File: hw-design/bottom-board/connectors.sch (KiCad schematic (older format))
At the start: 24 parts, among them J1 JACK_TRS_6PINS, J2 JACK_TRS_6PINS, J3 JACK_TRS_6PINS, J4 JACK_TRS_6PINS, J5 JACK_TRS_6PINS, J6 RJ45_LEDS, P5 BARREL_JACK, P6 HMI_POWER, P7 SD_CARD, P8 HMI_DATA, P9 SERIAL_DEBUG

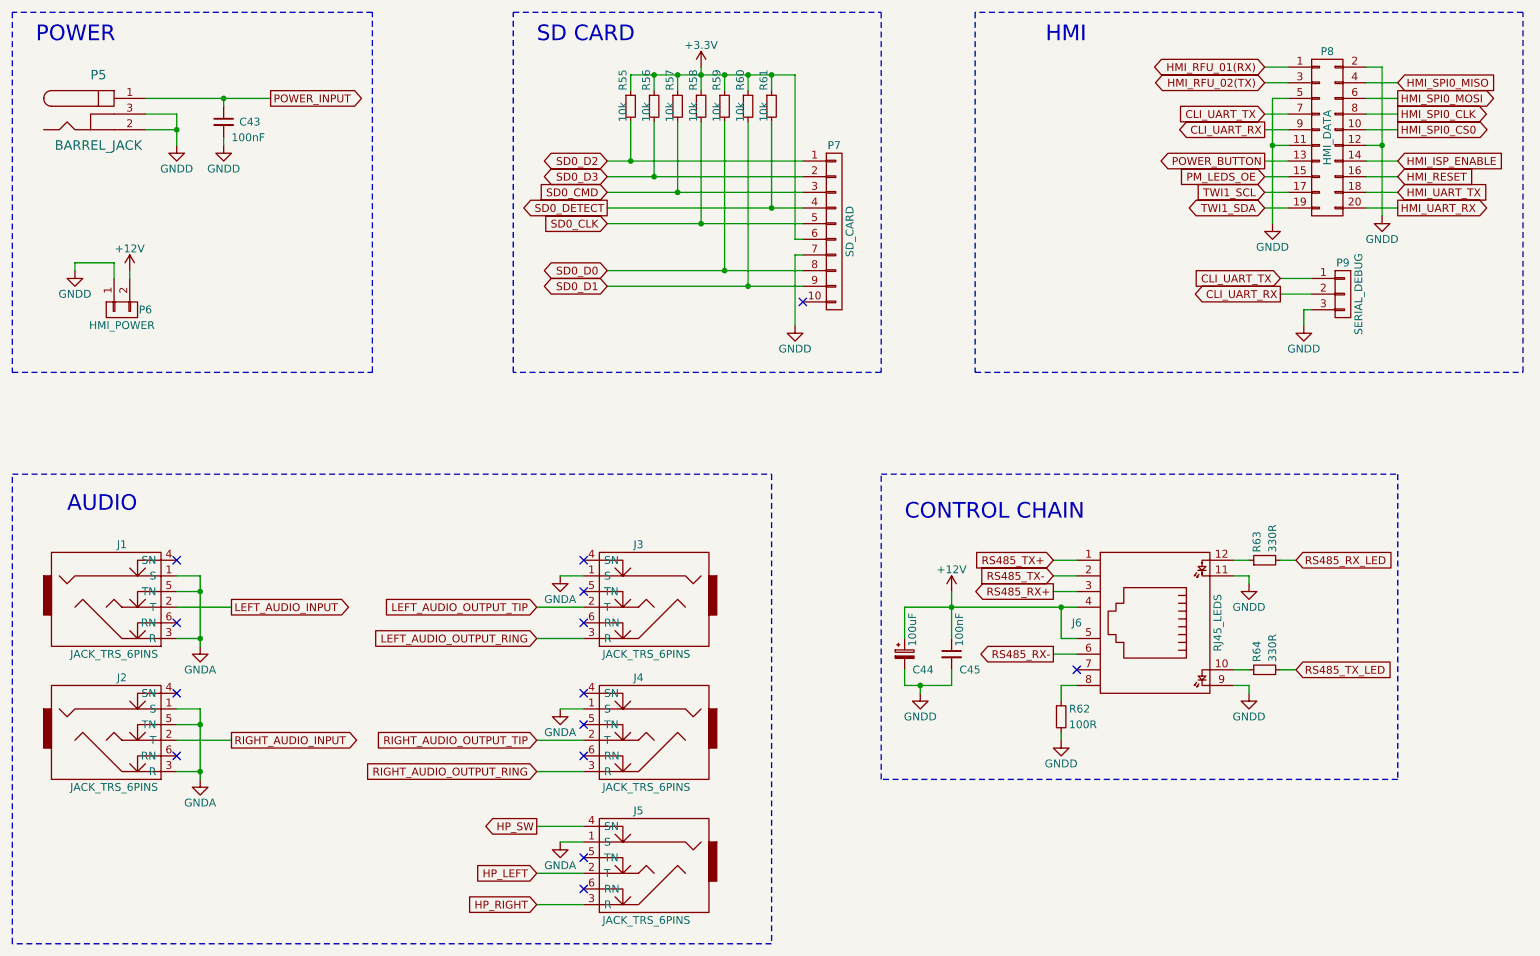
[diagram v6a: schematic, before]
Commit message: bottom-board,pcb: adding protection resistors to UART CLI
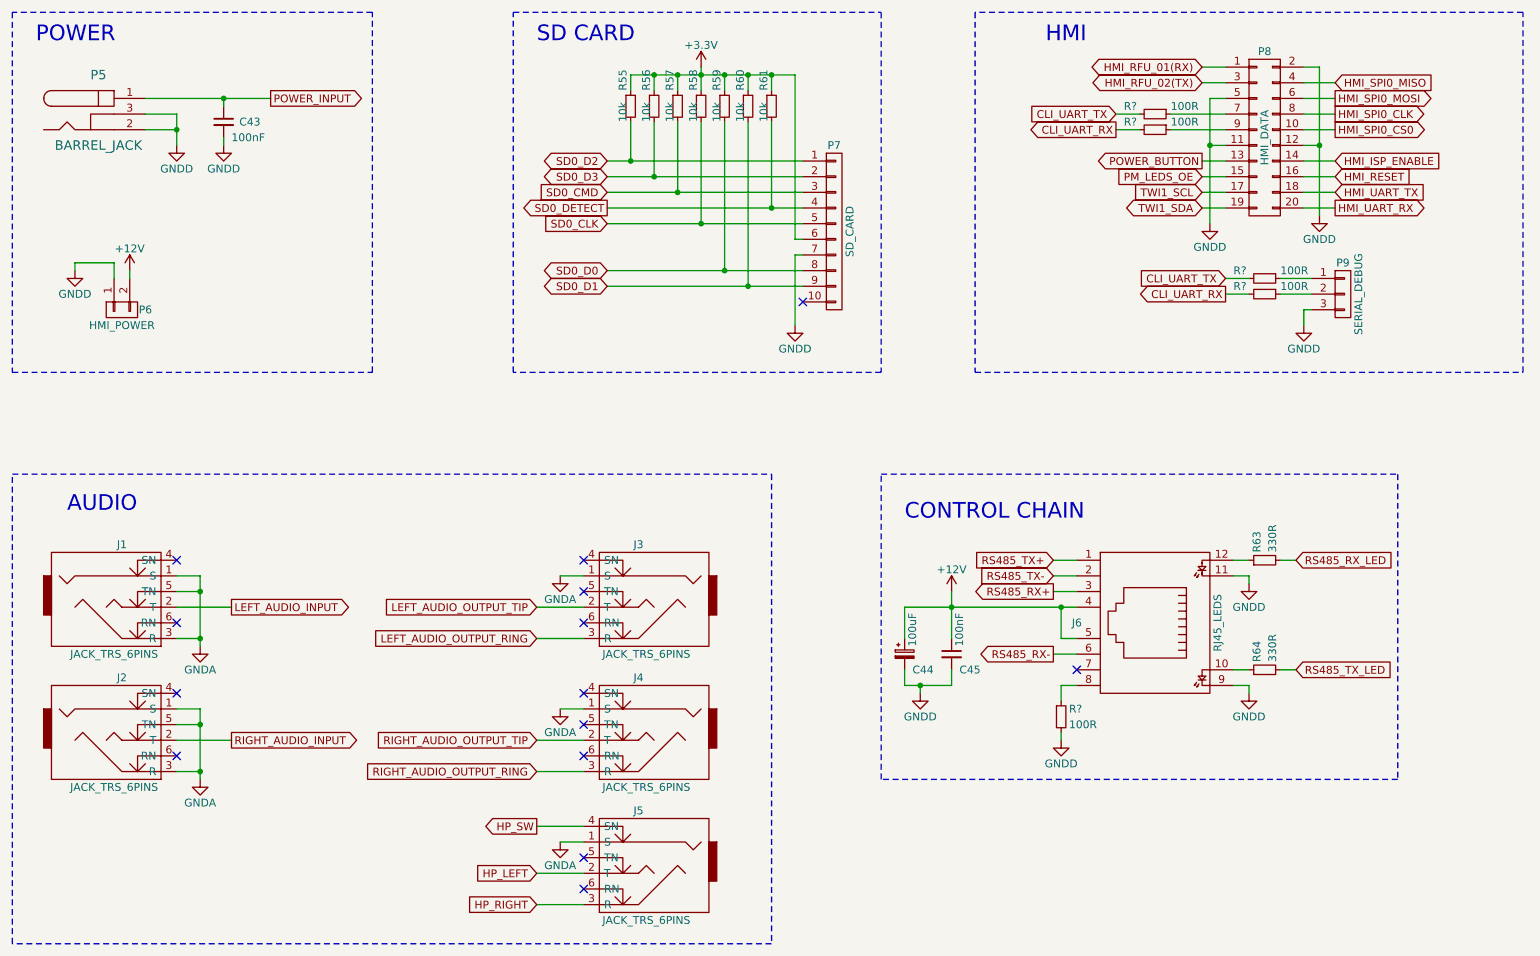
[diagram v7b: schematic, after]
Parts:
- removed R62: 100R, Resistors_SMD:R_0603, symbol R_Small
- added R? (x4): 100R, Resistors_SMD:R_0603, symbol R_Small
- added R?: 100R, Resistors_SMD:R_0805, symbol R_Small
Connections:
- net CLI_UART_RX: now also R?.2, R?.2; no longer P8.9 (P9), P9.2 (P2)
- net CLI_UART_TX: now also R?.2, R?.2; no longer P8.7 (P7), P9.1 (P1)
- net GNDD: now also R?.2
- net at J6.8: now also R?.1
- new net: P8.7 (P7), R?.1
- new net: P8.9 (P9), R?.1
- new net: P9.1 (P1), R?.1
- new net: P9.2 (P2), R?.1
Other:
- moved on the sheet: P8
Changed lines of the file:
@@
 L CONN_02X10 P8
 U 1 1 550C4B50
-P 9650 1650
-F 0 "P8" H 9650 2200 50  0000 C CNN
-F 1 "HMI_DATA" V 9650 1650 50  0000 C CNN
-F 2 "footprints:Pin_Header_Straight_2x10_Shrouded" H 9650 450 60  0001 C CNN
-F 3 "" H 9650 450 60  0000 C CNN
-F 4 "SBH11-PBPC-D10-ST-BK" H 450 -150 50  0001 C CNN "MPN"
-	1    9650 1650
+P 9250 1650
+F 0 "P8" H 9250 2200 50  0000 C CNN
+F 1 "HMI_DATA" V 9250 1650 50  0000 C CNN
+F 2 "footprints:Pin_Header_Straight_2x10_Shrouded" H 9250 450 60  0001 C CNN
+F 3 "" H 9250 450 60  0000 C CNN
+F 4 "SBH11-PBPC-D10-ST-BK" H 50  -150 50  0001 C CNN "MPN"
+	1    9250 1650
 	1    0    0    -1
 $EndComp
@@
 $EndComp
 $Comp
-L R_Small R62
-U 1 1 550C9A10
-P 7950 5350
-F 0 "R62" H 8000 5400 50  0000 L CNN
-F 1 "100R" H 8000 5300 50  0000 L CNN
-F 2 "Resistors_SMD:R_0603" H 7950 5350 60  0001 C CNN
-F 3 "" H 7950 5350 60  0000 C CNN
-F 4 "RMCF0603JT100R" H -800 0   50  0001 C CNN "MPN"
-	1    7950 5350
-	1    0    0    -1
-$EndComp
-$Comp
 L GNDD #PWR0152
 U 1 1 550C9AAB
@@
 L GNDD #PWR0161
 U 1 1 550AE498
-P 9300 2200
-F 0 "#PWR0161" H 9300 1950 50  0001 C CNN
-F 1 "GNDD" H 9300 2050 50  0000 C CNN
-F 2 "" H 9300 2200 60  0000 C CNN
-F 3 "" H 9300 2200 60  0000 C CNN
-	1    9300 2200
+P 8900 2200
+F 0 "#PWR0161" H 8900 1950 50  0001 C CNN
+F 1 "GNDD" H 8900 2050 50  0000 C CNN
+F 2 "" H 8900 2200 60  0000 C CNN
+F 3 "" H 8900 2200 60  0000 C CNN
+	1    8900 2200
 	1    0    0    -1
 $EndComp
@@
 L GNDD #PWR0162
 U 1 1 550B207C
-P 10000 2150
-F 0 "#PWR0162" H 10000 1900 50  0001 C CNN
-F 1 "GNDD" H 10000 2000 50  0000 C CNN
-F 2 "" H 10000 2150 60  0000 C CNN
-F 3 "" H 10000 2150 60  0000 C CNN
-	1    10000 2150
+P 9600 2150
+F 0 "#PWR0162" H 9600 1900 50  0001 C CNN
+F 1 "GNDD" H 9600 2000 50  0000 C CNN
+F 2 "" H 9600 2150 60  0000 C CNN
+F 3 "" H 9600 2150 60  0000 C CNN
+	1    9600 2150
 	1    0    0    -1
 $EndComp
@@
 Text Notes 7850 1050 0    100  ~ 0
 HMI
-Text GLabel 9350 2550 0    50   Input ~ 0
+Text GLabel 9000 2550 0    50   Input ~ 0
 CLI_UART_TX
-Text GLabel 9350 2650 0    50   Output ~ 0
+Text GLabel 9000 2650 0    50   Output ~ 0
 CLI_UART_RX
-Text GLabel 10100 2100 2    50   Output ~ 0
+Text GLabel 9700 2100 2    50   Output ~ 0
 HMI_UART_RX
-Text GLabel 10100 2000 2    50   Input ~ 0
+Text GLabel 9700 2000 2    50   Input ~ 0
 HMI_UART_TX
-Text GLabel 10100 1800 2    50   Input ~ 0
+Text GLabel 9700 1800 2    50   Input ~ 0
 HMI_ISP_ENABLE
-Text GLabel 10100 1900 2    50   Input ~ 0
+Text GLabel 9700 1900 2    50   Input ~ 0
 HMI_RESET
-Text GLabel 9250 1500 0    50   Input ~ 0
+Text GLabel 8300 1500 0    50   Input ~ 0
 CLI_UART_TX
-Text GLabel 9250 1600 0    50   Output ~ 0
+Text GLabel 8300 1600 0    50   Output ~ 0
 CLI_UART_RX
 Text GLabel 5050 2200 0    50   Input ~ 0
@@
 Text Notes 4600 1050 0    100  ~ 0
 SD CARD
-Text GLabel 10100 1300 2    50   Input ~ 0
+Text GLabel 9700 1300 2    50   Input ~ 0
 HMI_SPI0_MISO
-Text GLabel 10100 1500 2    50   Output ~ 0
+Text GLabel 9700 1500 2    50   Output ~ 0
 HMI_SPI0_CLK
-Text GLabel 10100 1600 2    50   Output ~ 0
+Text GLabel 9700 1600 2    50   Output ~ 0
 HMI_SPI0_CS0
-Text GLabel 10100 1400 2    50   Output ~ 0
+Text GLabel 9700 1400 2    50   Output ~ 0
 HMI_SPI0_MOSI
-Text GLabel 9250 1800 0    50   Output ~ 0
+Text GLabel 8850 1800 0    50   Output ~ 0
 POWER_BUTTON
 Text GLabel 9450 5050 2    50   Input ~ 0
@@
 Text GLabel 9450 4350 2    50   Input ~ 0
 RS485_RX_LED
-Text GLabel 9250 2100 0    50   BiDi ~ 0
+Text GLabel 8850 2100 0    50   BiDi ~ 0
 TWI1_SDA
-Text GLabel 9250 2000 0    50   Input ~ 0
+Text GLabel 8850 2000 0    50   Input ~ 0
 TWI1_SCL
-Text GLabel 9250 1200 0    50   BiDi ~ 0
+Text GLabel 8850 1200 0    50   BiDi ~ 0
 HMI_RFU_01(RX)
-Text GLabel 9250 1300 0    50   BiDi ~ 0
+Text GLabel 8850 1300 0    50   BiDi ~ 0
 HMI_RFU_02(TX)
-Text GLabel 9250 1900 0    50   Input ~ 0
+Text GLabel 8850 1900 0    50   Input ~ 0
 PM_LEDS_OE
 Wire Wire Line
@@
 	2450 5300 2300 5300
 Wire Wire Line
-	2300 4850 2450 4850
+	2450 4850 2300 4850
 Wire Wire Line
 	2450 4450 2450 4900
@@
 	2300 4450 2450 4450
 Wire Wire Line
-	2300 5700 2450 5700
+	2450 5700 2300 5700
 Wire Wire Line
 	2450 5300 2450 5750
@@
 	6800 5750 6800 3800
 Wire Wire Line
-	9250 1600 9400 1600
-Wire Wire Line
-	9400 1500 9250 1500
-Wire Wire Line
-	10100 1900 9900 1900
-Wire Wire Line
-	9900 1800 10100 1800
-Wire Wire Line
-	10100 2100 9900 2100
-Wire Wire Line
-	9900 2000 10100 2000
+	8650 1600 9000 1600
+Wire Wire Line
+	9000 1500 8650 1500
+Wire Wire Line
+	9700 1900 9500 1900
+Wire Wire Line
+	9500 1800 9700 1800
+Wire Wire Line
+	9700 2100 9500 2100
+Wire Wire Line
+	9500 2000 9700 2000
 Wire Notes Line
 	7400 850  7400 3150
@@
 	4450 3150 4450 850
 Wire Wire Line
-	10100 1300 9900 1300
-Wire Wire Line
-	9900 1400 10100 1400
-Wire Wire Line
-	10100 1500 9900 1500
-Wire Wire Line
-	9900 1600 10100 1600
-Wire Wire Line
-	10000 1200 10000 2150
-Wire Wire Line
-	9900 1700 10000 1700
-Wire Wire Line
-	9400 1300 9250 1300
-Wire Wire Line
-	10000 1200 9900 1200
+	9700 1300 9500 1300
+Wire Wire Line
+	9500 1400 9700 1400
+Wire Wire Line
+	9700 1500 9500 1500
+Wire Wire Line
+	9500 1600 9700 1600
+Wire Wire Line
+	9600 1200 9600 2150
+Wire Wire Line
+	9500 1700 9600 1700
+Wire Wire Line
+	9000 1300 8850 1300
+Wire Wire Line
+	9600 1200 9500 1200
 Wire Wire Line
 	7950 4850 8050 4850
@@
 	1900 2450 1900 2550
 Wire Wire Line
-	9250 1200 9400 1200
-Wire Wire Line
-	9400 1400 9300 1400
-Wire Wire Line
-	9300 1400 9300 2200
-Wire Wire Line
-	9250 2000 9400 2000
-Wire Wire Line
-	9250 2100 9400 2100
-Wire Wire Line
-	9400 1700 9300 1700
-Wire Wire Line
-	9400 1800 9250 1800
-Wire Wire Line
-	9250 1900 9400 1900
+	8850 1200 9000 1200
+Wire Wire Line
+	9000 1400 8900 1400
+Wire Wire Line
+	8900 1400 8900 2200
+Wire Wire Line
+	8850 2000 9000 2000
+Wire Wire Line
+	8850 2100 9000 2100
+Wire Wire Line
+	9000 1700 8900 1700
+Wire Wire Line
+	9000 1800 8850 1800
+Wire Wire Line
+	8850 1900 9000 1900
 Connection ~ 2300 1600
 Connection ~ 2600 1400
@@
 Connection ~ 5950 1250
 Connection ~ 6100 1250
-Connection ~ 10000 1700
-Connection ~ 9300 1700
+Connection ~ 9600 1700
+Connection ~ 8900 1700
 NoConn ~ 8050 5050
 NoConn ~ 4900 6450
@@
 	2300 4550 2450 4550
 Connection ~ 2450 4550
+$Comp
+L R_Small R?
+U 1 1 566413AE
+P 9250 2550
+F 0 "R?" V 9200 2350 50  0000 L CNN
+F 1 "100R" V 9200 2650 50  0000 L CNN
+F 2 "Resistors_SMD:R_0603" H 9250 2550 60  0001 C CNN
+F 3 "" H 9250 2550 60  0000 C CNN
+F 4 "RMCF0603JT100R" H 500 -2800 50  0001 C CNN "MPN"
+	1    9250 2550
+	0    1    1    0
+$EndComp
+$Comp
+L R_Small R?
+U 1 1 56642329
+P 9250 2650
+F 0 "R?" V 9200 2450 50  0000 L CNN
+F 1 "100R" V 9200 2750 50  0000 L CNN
+F 2 "Resistors_SMD:R_0603" H 9250 2650 60  0001 C CNN
+F 3 "" H 9250 2650 60  0000 C CNN
+F 4 "RMCF0603JT100R" H 500 -2700 50  0001 C CNN "MPN"
+	1    9250 2650
+	0    1    1    0
+$EndComp
+Wire Wire Line
+	9000 2550 9150 2550
+Wire Wire Line
+	9000 2650 9150 2650
+$Comp
+L R_Small R?
+U 1 1 566433EA
+P 8550 1500
+F 0 "R?" V 8500 1300 50  0000 L CNN
+F 1 "100R" V 8500 1600 50  0000 L CNN
+F 2 "Resistors_SMD:R_0603" H 8550 1500 60  0001 C CNN
+F 3 "" H 8550 1500 60  0000 C CNN
+F 4 "RMCF0603JT100R" H -200 -3850 50  0001 C CNN "MPN"
+	1    8550 1500
+	0    1    1    0
+$EndComp
+$Comp
+L R_Small R?
+U 1 1 566433F1
+P 8550 1600
+F 0 "R?" V 8500 1400 50  0000 L CNN
+F 1 "100R" V 8500 1700 50  0000 L CNN
+F 2 "Resistors_SMD:R_0603" H 8550 1600 60  0001 C CNN
+F 3 "" H 8550 1600 60  0000 C CNN
+F 4 "RMCF0603JT100R" H -200 -3750 50  0001 C CNN "MPN"
+	1    8550 1600
+	0    1    1    0
+$EndComp
+Wire Wire Line
+	8450 1500 8300 1500
+Wire Wire Line
+	8300 1600 8450 1600
+$Comp
+L R_Small R?
+U 1 1 56645EF2
+P 7950 5350
+F 0 "R?" H 8000 5400 50  0000 L CNN
+F 1 "100R" H 8000 5300 50  0000 L CNN
+F 2 "Resistors_SMD:R_0805" H 7950 5350 60  0001 C CNN
+F 3 "" H 7950 5350 60  0000 C CNN
+F 4 "ERJ-P06J101V" H 1400 3050 50  0001 C CNN "MPN"
+	1    7950 5350
+	1    0    0    -1
+$EndComp
 $EndSCHEMATC
